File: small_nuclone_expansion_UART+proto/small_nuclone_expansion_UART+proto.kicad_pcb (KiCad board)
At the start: 2 copper layers, 50 x 50 mm, 64 parts, among them J1 USB-C_PD_USB, J3 nuclone_small_left, J4 nuclone_small_right, U1 TPESD0504C6, U2 CH340B

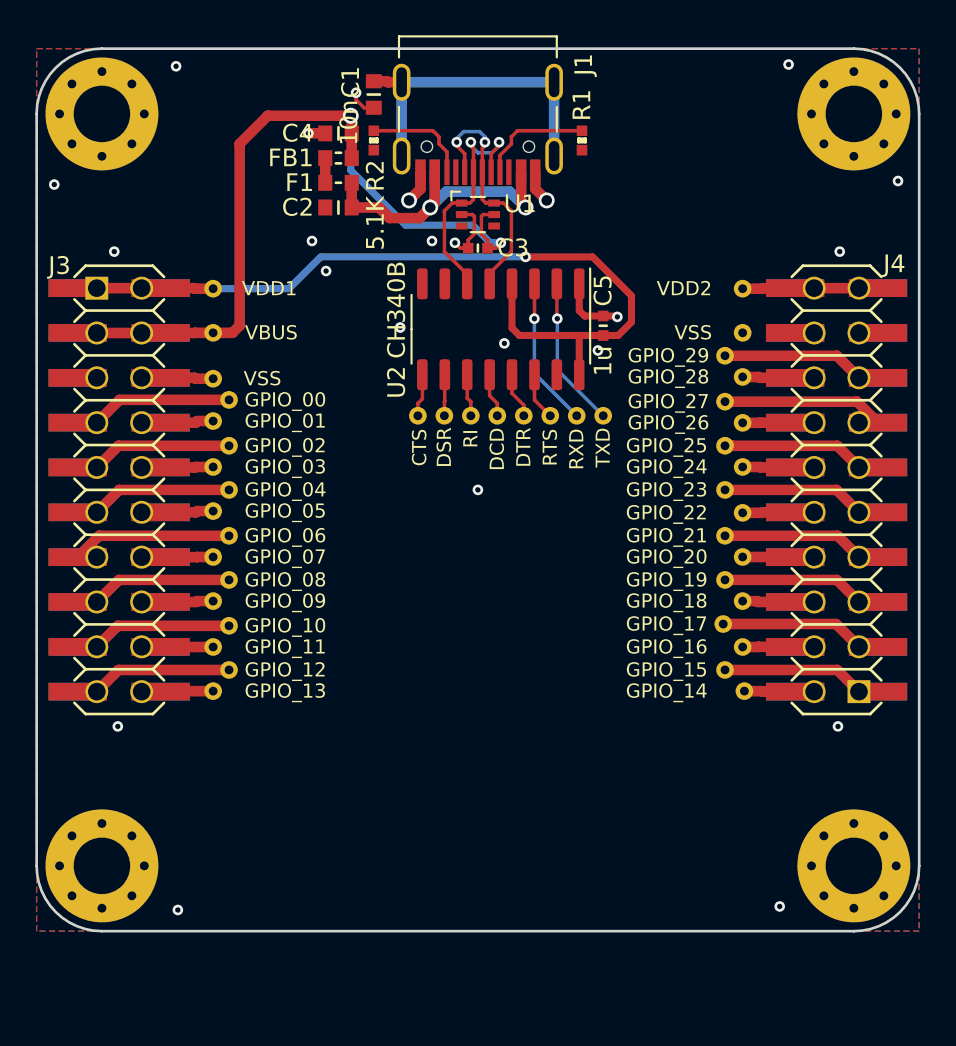
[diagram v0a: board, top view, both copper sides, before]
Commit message: Added breakout connection and prototyping area
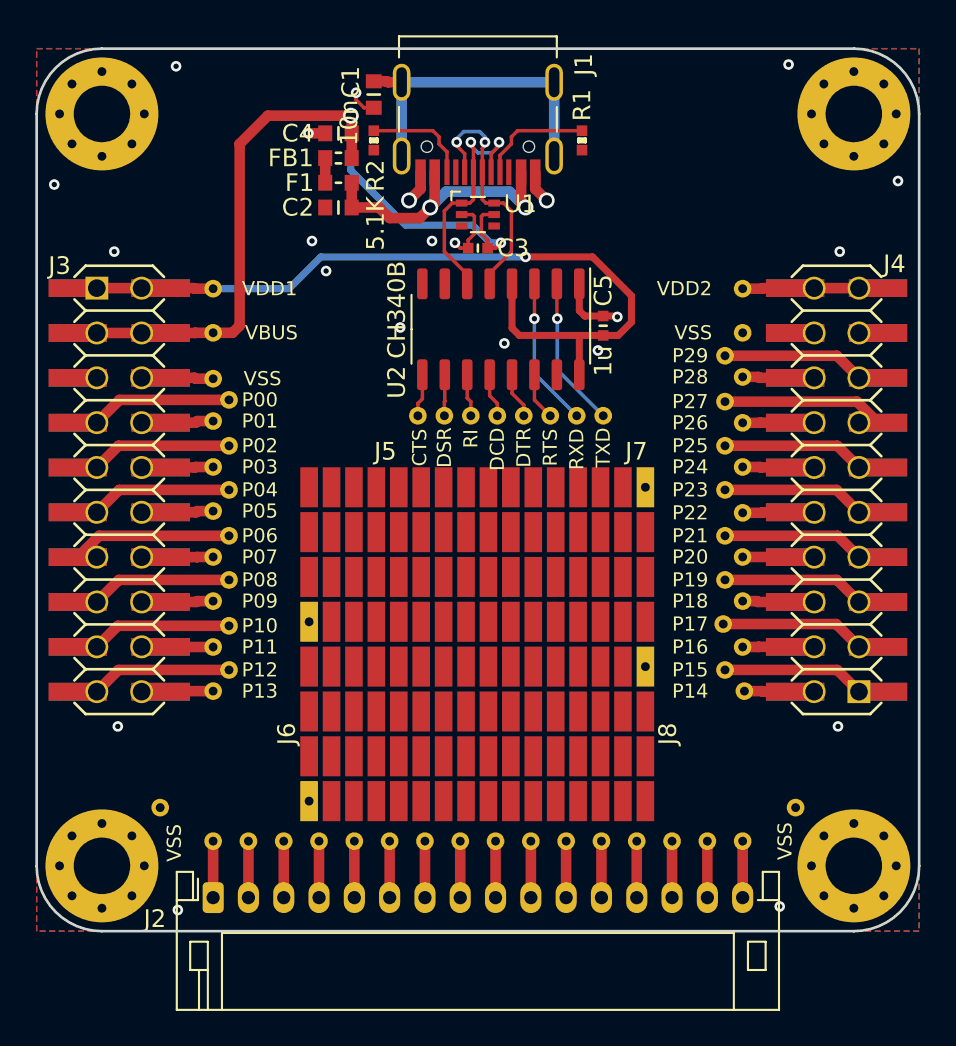
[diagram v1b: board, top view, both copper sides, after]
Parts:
- added J2: Conn_01x16, Connector_JST:JST_PH_S16B-PH-K_1x16_P2.00mm_Horizontal, F.Cu at (70.0, 109.1)
- added J5: 127, SquantorProto:proto-SMD-0127-08X08-P010X020+pin, F.Cu at (79.9, 89.7)
- added J6: 127, SquantorProto:proto-SMD-0127-08X08-P010X020+pin, F.Cu at (79.9, 99.8)
- added J7: 127, SquantorProto:proto-SMD-0127-08X08-P010X020+pin, F.Cu at (90.0, 89.7)
- added J8: 127, SquantorProto:proto-SMD-0127-08X08-P010X020+pin, F.Cu at (90.0, 99.8)
- added TP44: PH1, SquantorTestPoints:TestPoint_hole_H05R10_small_text, F.Cu at (70.0, 105.9)
- added TP45: PH2, SquantorTestPoints:TestPoint_hole_H05R10_small_text, F.Cu at (72.0, 105.9)
- added TP46: PH3, SquantorTestPoints:TestPoint_hole_H05R10_small_text, F.Cu at (74.0, 105.9)
- added TP47: PH4, SquantorTestPoints:TestPoint_hole_H05R10_small_text, F.Cu at (76.0, 105.9)
- added TP48: PH5, SquantorTestPoints:TestPoint_hole_H05R10_small_text, F.Cu at (78.0, 105.9)
- added TP49: PH6, SquantorTestPoints:TestPoint_hole_H05R10_small_text, F.Cu at (80.0, 105.9)
- added TP50: PH7, SquantorTestPoints:TestPoint_hole_H05R10_small_text, F.Cu at (82.0, 105.9)
- added TP51: PH8, SquantorTestPoints:TestPoint_hole_H05R10_small_text, F.Cu at (84.0, 105.9)
- added TP52: PH9, SquantorTestPoints:TestPoint_hole_H05R10_small_text, F.Cu at (86.0, 105.9)
- added TP53: PH10, SquantorTestPoints:TestPoint_hole_H05R10_small_text, F.Cu at (88.0, 105.9)
- added TP54: PH11, SquantorTestPoints:TestPoint_hole_H05R10_small_text, F.Cu at (90.0, 105.9)
- added TP55: PH12, SquantorTestPoints:TestPoint_hole_H05R10_small_text, F.Cu at (92.0, 105.9)
- added TP56: PH13, SquantorTestPoints:TestPoint_hole_H05R10_small_text, F.Cu at (94.0, 105.9)
- added TP57: PH14, SquantorTestPoints:TestPoint_hole_H05R10_small_text, F.Cu at (96.0, 105.9)
- added TP58: PH15, SquantorTestPoints:TestPoint_hole_H05R10_small_text, F.Cu at (98.0, 105.9)
- added TP59: PH16, SquantorTestPoints:TestPoint_hole_H05R10_small_text, F.Cu at (100.0, 105.9)
- added TP60: VSS, SquantorTestPoints:TestPoint_hole_H05R10_small_text, F.Cu at (103.0, 104.0)
- added TP61: VSS, SquantorTestPoints:TestPoint_hole_H05R10_small_text, F.Cu at (67.0, 104.0)
- TP10: value GPIO_06 -> P06
- TP11: value GPIO_07 -> P07
- TP12: value GPIO_08 -> P08
- TP13: value GPIO_09 -> P09
- TP14: value GPIO_10 -> P10
- TP15: value GPIO_11 -> P11
- TP16: value GPIO_12 -> P12
- TP17: value GPIO_13 -> P13
- TP20: value GPIO_29 -> P29
- TP21: value GPIO_28 -> P28
- TP22: value GPIO_27 -> P27
- TP23: value GPIO_26 -> P26
- TP24: value GPIO_25 -> P25
- TP25: value GPIO_24 -> P24
- TP26: value GPIO_23 -> P23
- TP27: value GPIO_22 -> P22
- TP28: value GPIO_21 -> P21
- TP29: value GPIO_20 -> P20
- TP30: value GPIO_19 -> P19
- TP31: value GPIO_18 -> P18
- TP32: value GPIO_17 -> P17
- TP33: value GPIO_16 -> P16
- TP34: value GPIO_15 -> P15
- TP35: value GPIO_14 -> P14
- TP4: value GPIO_00 -> P00
- TP5: value GPIO_01 -> P01
- TP6: value GPIO_02 -> P02
- TP7: value GPIO_03 -> P03
- TP8: value GPIO_04 -> P04
- TP9: value GPIO_05 -> P05
- moved N1 9.40 mm to (85.0, 94.2)
- moved N2 9.40 mm to (85.1, 98.0)
- moved N3 9.40 mm to (85.0, 99.5)
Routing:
- net Net-(J2-Pad9): track 0.00 -> 3.20 mm
- net Net-(J2-Pad8): track 0.00 -> 3.20 mm
- net Net-(J2-Pad7): track 0.00 -> 3.20 mm
- net Net-(J2-Pad6): track 0.00 -> 3.20 mm
- net Net-(J2-Pad5): track 0.00 -> 3.20 mm
- net Net-(J2-Pad4): track 0.00 -> 3.20 mm
- net Net-(J2-Pad3): track 0.00 -> 3.20 mm
- net Net-(J2-Pad2): track 0.00 -> 3.20 mm
- net Net-(J2-Pad16): track 0.00 -> 3.20 mm
- net Net-(J2-Pad15): track 0.00 -> 3.20 mm
- net Net-(J2-Pad14): track 0.00 -> 3.20 mm
- net Net-(J2-Pad13): track 0.00 -> 3.20 mm
- net Net-(J2-Pad12): track 0.00 -> 3.20 mm
- net Net-(J2-Pad11): track 0.00 -> 3.20 mm
- net Net-(J2-Pad10): track 0.00 -> 3.20 mm
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
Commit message: updated prototyping area
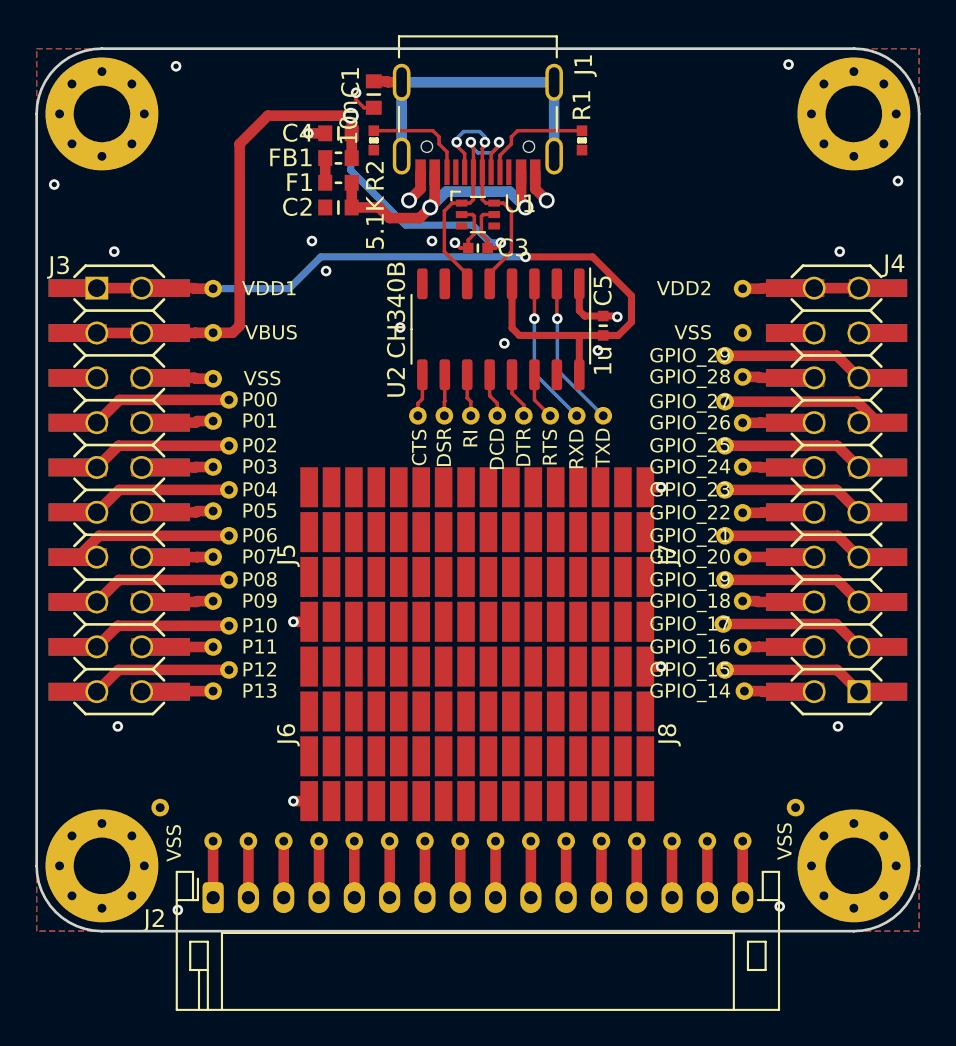
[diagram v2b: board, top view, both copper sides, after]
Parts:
- J5, J6, J7, J8: footprint SquantorProto:proto-SMD-0127-08X08-P010X020+pin -> SquantorProto:proto-SMD-0127-08X08-P010X020+pad
- TP20: value P29 -> GPIO_29
- TP21: value P28 -> GPIO_28
- TP22: value P27 -> GPIO_27
- TP23: value P26 -> GPIO_26
- TP24: value P25 -> GPIO_25
- TP25: value P24 -> GPIO_24
- TP26: value P23 -> GPIO_23
- TP27: value P22 -> GPIO_22
- TP28: value P21 -> GPIO_21
- TP29: value P20 -> GPIO_20
- TP30: value P19 -> GPIO_19
- TP31: value P18 -> GPIO_18
- TP32: value P17 -> GPIO_17
- TP33: value P16 -> GPIO_16
- TP34: value P15 -> GPIO_15
- TP35: value P14 -> GPIO_14
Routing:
- net /VSS: track 16.7 -> 20.2 mm, vias 22 -> 26

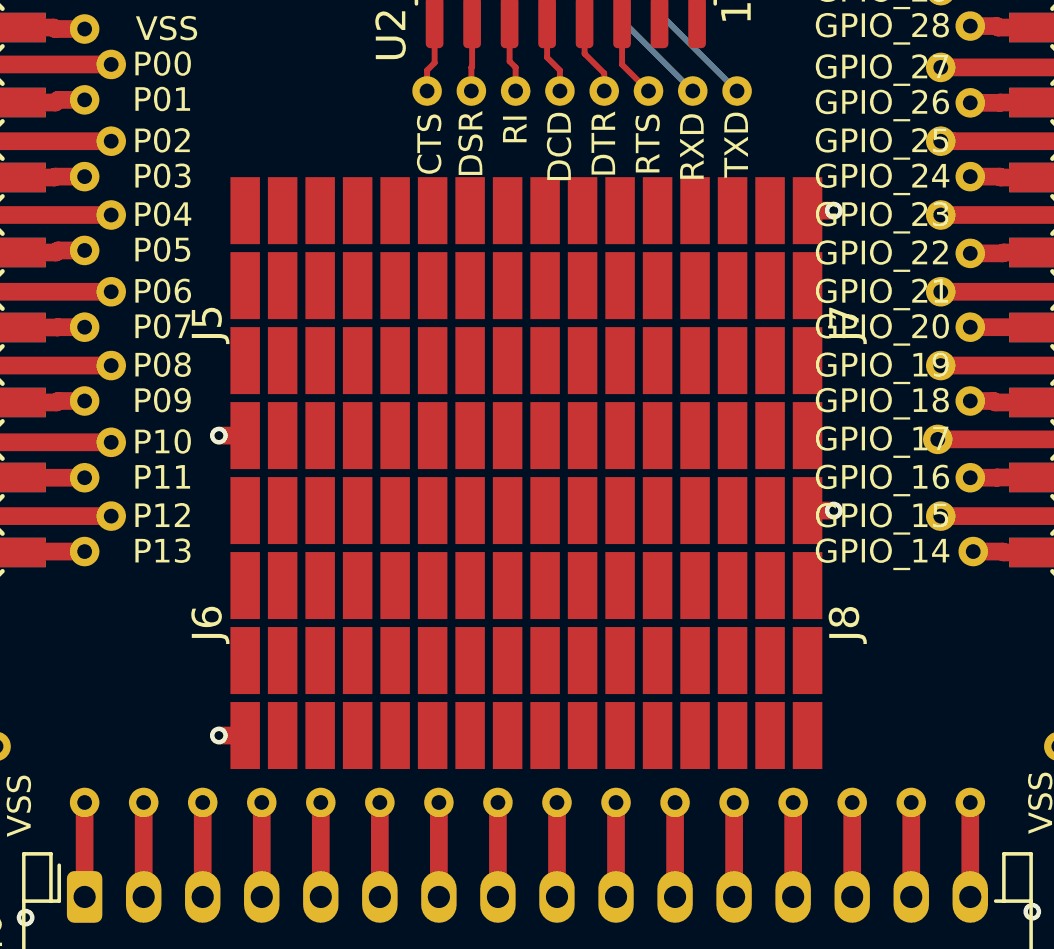
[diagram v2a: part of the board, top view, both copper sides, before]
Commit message: updated footprints for prototyping area
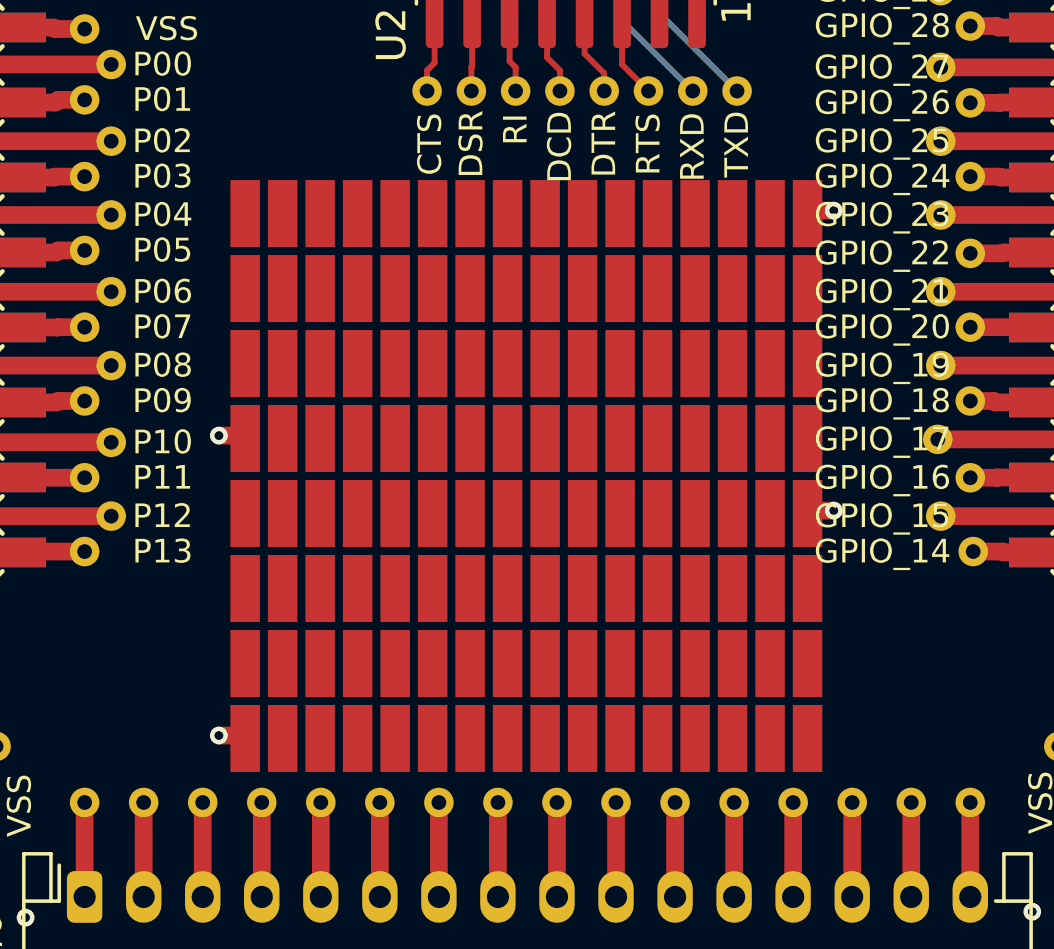
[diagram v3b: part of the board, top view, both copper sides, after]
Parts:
- moved J5 0.10 mm to (79.9, 89.8)
- moved J6 0.10 mm to (79.9, 99.9)
- moved J7 0.10 mm to (90.0, 89.8)
- moved J8 0.10 mm to (90.0, 99.9)
